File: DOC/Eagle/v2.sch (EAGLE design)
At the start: 18 parts, among them M1 RF-LORA-868-SO, X1 SMA-142-0701-871/876

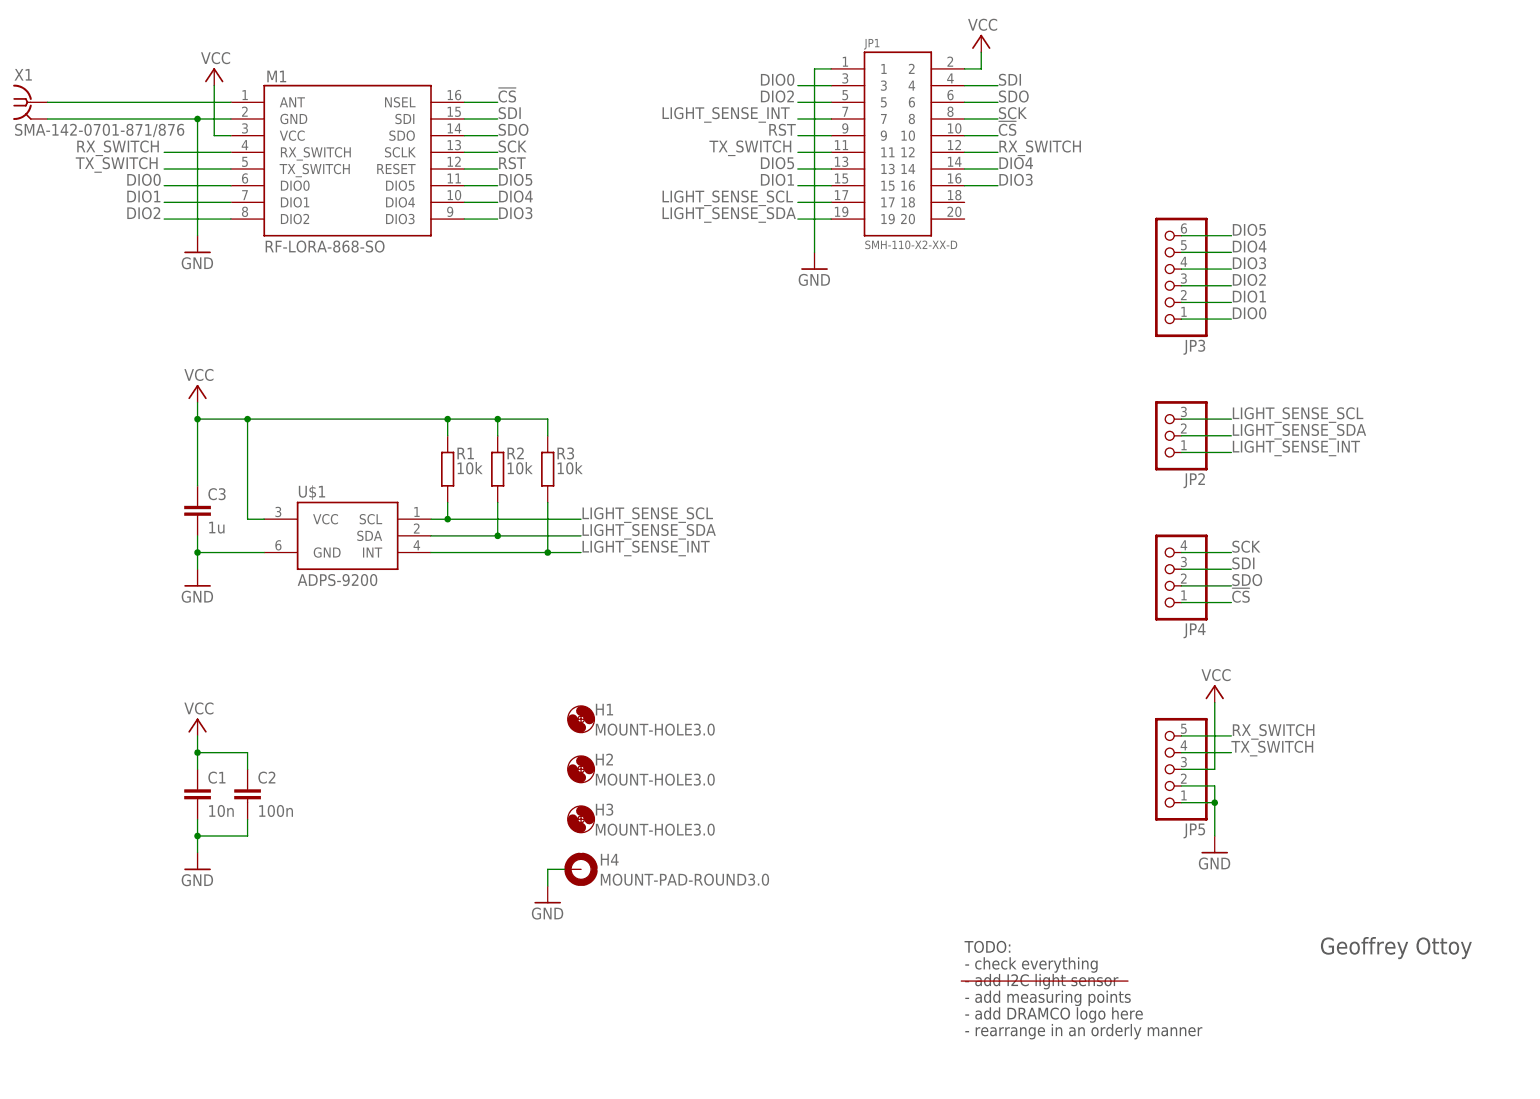
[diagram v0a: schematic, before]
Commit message: Updated hardware design
Finished schematic (final checks needed!)
Included pdf of the schematic
First version of the board (no silkscreen yet)
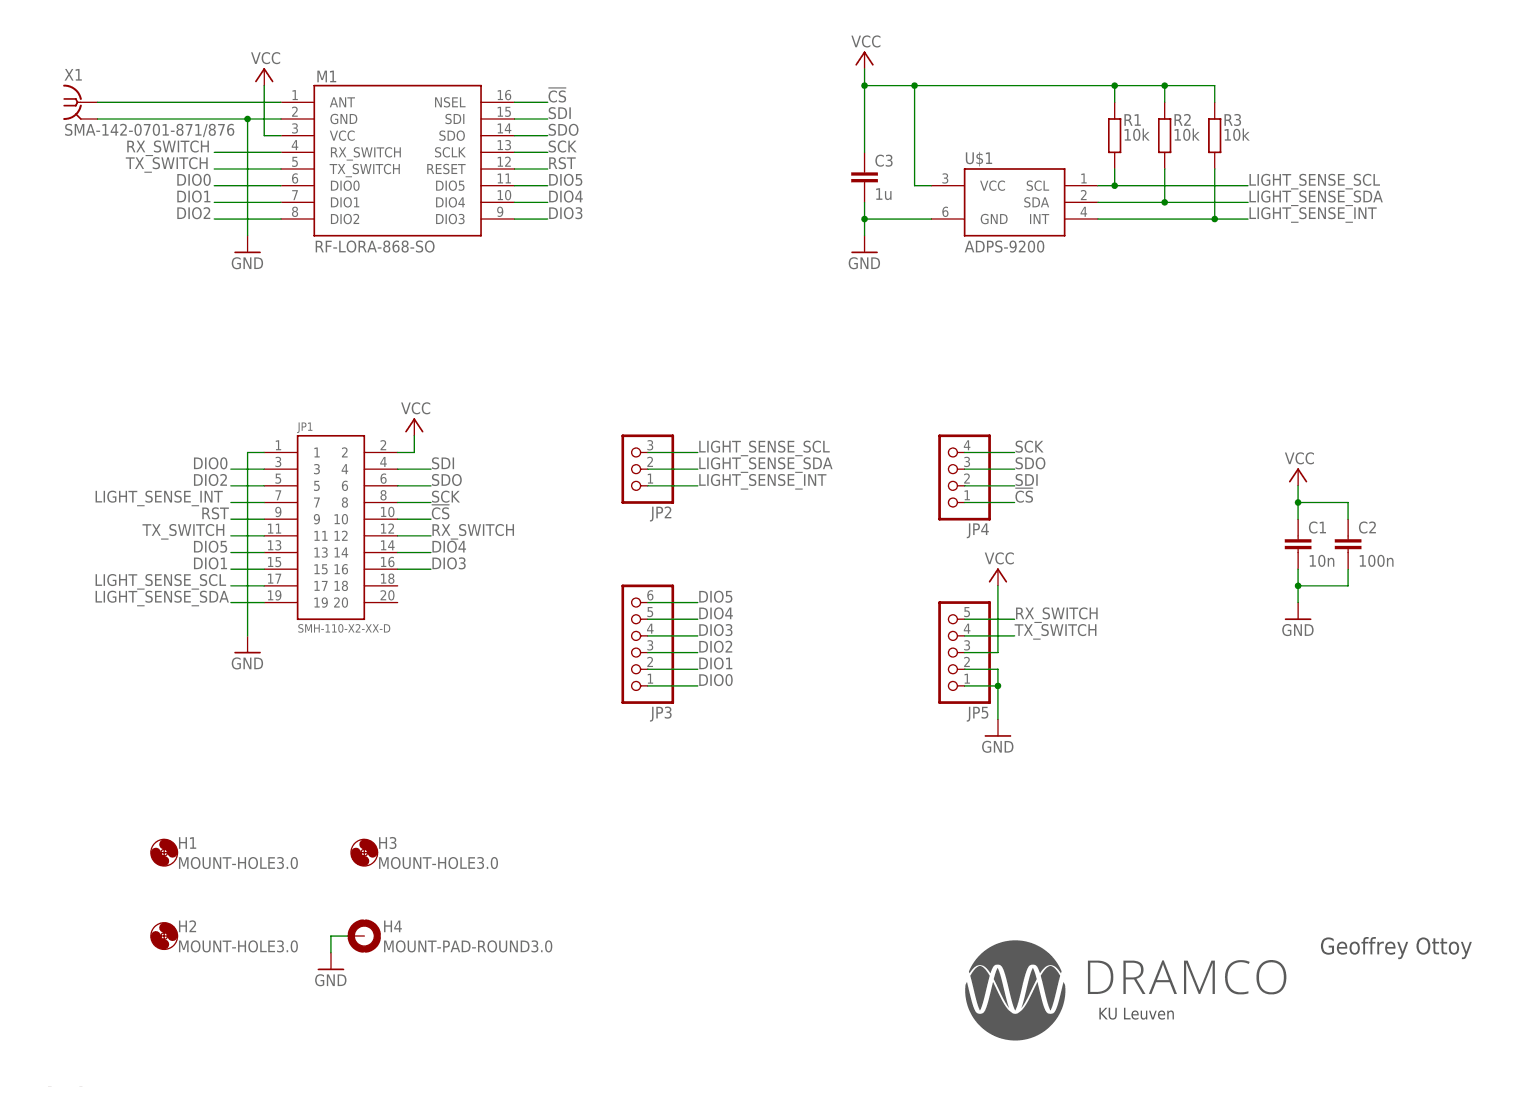
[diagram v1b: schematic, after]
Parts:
- R1, R2, R3: device rcl:R-EU_R1206 -> rcl:R-EU_M0805
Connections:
- net SDI: now also JP4.2; no longer JP4.3
- net SDO: now also JP4.3; no longer JP4.2
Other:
- note added: "KU Leuven"
- note removed: "- add DRAMCO logo here"
- note removed: "- add I2C light sensor"
- note removed: "- add measuring points"
- note removed: "- check everything"
- note removed: "- rearrange in an orderly manner"
- note removed: "TODO:"
- moved on the sheet: C1, C2, C3, H1, H2, H3, H4, JP1, JP2, JP3, JP4, JP5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

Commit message: Updated board design
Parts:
- H1, H2, H3: value MOUNT-HOLE3.0 -> MOUNT-PAD-ROUND3.0; device holes:MOUNT-HOLE3.0 -> holes:MOUNT-PAD-ROUND3.0
- renumbered U$1 to IC1
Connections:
- net GND: now also H1.MOUNT, H2.MOUNT, H3.MOUNT
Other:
- moved on the sheet: H2, H3, H4
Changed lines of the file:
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@@
 </classes>
 <parts>
-<part name="H1" library="holes" library_urn="urn:adsk.eagle:library:237" deviceset="MOUNT-HOLE" device="3.0"/>
-<part name="H2" library="holes" library_urn="urn:adsk.eagle:library:237" deviceset="MOUNT-HOLE" device="3.0"/>
-<part name="H3" library="holes" library_urn="urn:adsk.eagle:library:237" deviceset="MOUNT-HOLE" device="3.0"/>
 <part name="H4" library="holes" library_urn="urn:adsk.eagle:library:237" deviceset="MOUNT-PAD-ROUND" device="3.0"/>
 <part name="GND1" library="supply1" library_urn="urn:adsk.eagle:library:371" deviceset="GND" device=""/>
@@
 <part name="R2" library="rcl" library_urn="urn:adsk.eagle:library:334" deviceset="R-EU_" device="M0805" value="10k"/>
 <part name="R3" library="rcl" library_urn="urn:adsk.eagle:library:334" deviceset="R-EU_" device="M0805" value="10k"/>
-<part name="U$1" library="project" deviceset="ADPS-9200" device=""/>
 <part name="C3" library="rcl" library_urn="urn:adsk.eagle:library:334" deviceset="C-EU" device="C0805K" value="1u"/>
 <part name="GND5" library="supply1" library_urn="urn:adsk.eagle:library:371" deviceset="GND" device=""/>
@@
 <part name="P+5" library="supply1" library_urn="urn:adsk.eagle:library:371" deviceset="VCC" device=""/>
 <part name="GND6" library="supply1" library_urn="urn:adsk.eagle:library:371" deviceset="GND" device=""/>
+<part name="IC1" library="project" deviceset="ADPS-9200" device=""/>
+<part name="H2" library="holes" library_urn="urn:adsk.eagle:library:237" deviceset="MOUNT-PAD-ROUND" device="3.0"/>
+<part name="H3" library="holes" library_urn="urn:adsk.eagle:library:237" deviceset="MOUNT-PAD-ROUND" device="3.0"/>
+<part name="H1" library="holes" library_urn="urn:adsk.eagle:library:237" deviceset="MOUNT-PAD-ROUND" device="3.0"/>
+<part name="GND7" library="supply1" library_urn="urn:adsk.eagle:library:371" deviceset="GND" device=""/>
+<part name="GND8" library="supply1" library_urn="urn:adsk.eagle:library:371" deviceset="GND" device=""/>
+<part name="GND9" library="supply1" library_urn="urn:adsk.eagle:library:371" deviceset="GND" device=""/>
 </parts>
 <sheets>
@@
 </plain>
 <instances>
-<instance part="H1" gate="G$1" x="40.64" y="35.56"/>
-<instance part="H2" gate="G$1" x="40.64" y="22.86"/>
-<instance part="H3" gate="G$1" x="71.12" y="35.56"/>
-<instance part="H4" gate="G$1" x="71.12" y="22.86"/>
-<instance part="GND1" gate="1" x="66.04" y="17.78"/>
+<instance part="H4" gate="G$1" x="78.74" y="22.86"/>
+<instance part="GND1" gate="1" x="73.66" y="17.78"/>
 <instance part="JP1" gate="G$1" x="66.04" y="86.36"/>
 <instance part="GND2" gate="1" x="53.34" y="66.04"/>
@@
 <attribute name="VALUE" x="201.93" y="144.018" size="1.778" layer="96"/>
 </instance>
-<instance part="U$1" gate="G$1" x="170.18" y="134.62"/>
 <instance part="C3" gate="G$1" x="147.32" y="139.7"/>
 <instance part="GND5" gate="1" x="147.32" y="127"/>
@@
 </instance>
 <instance part="GND6" gate="1" x="167.64" y="53.34"/>
+<instance part="IC1" gate="G$1" x="170.18" y="134.62"/>
+<instance part="H2" gate="G$1" x="78.74" y="35.56"/>
+<instance part="H3" gate="G$1" x="40.64" y="22.86"/>
+<instance part="H1" gate="G$1" x="40.64" y="35.56"/>
+<instance part="GND7" gate="1" x="73.66" y="30.48"/>
+<instance part="GND8" gate="1" x="35.56" y="30.48"/>
+<instance part="GND9" gate="1" x="35.56" y="17.78"/>
 </instances>
 <busses>
@@
 <pinref part="H4" gate="G$1" pin="MOUNT"/>
 <pinref part="GND1" gate="1" pin="GND"/>
-<wire x1="68.58" y1="22.86" x2="66.04" y2="22.86" width="0.1524" layer="91"/>
-<wire x1="66.04" y1="22.86" x2="66.04" y2="20.32" width="0.1524" layer="91"/>
+<wire x1="76.2" y1="22.86" x2="73.66" y2="22.86" width="0.1524" layer="91"/>
+<wire x1="73.66" y1="22.86" x2="73.66" y2="20.32" width="0.1524" layer="91"/>
 </segment>
 <segment>
@@
 </segment>
 <segment>
-<pinref part="U$1" gate="G$1" pin="GND"/>
 <wire x1="157.48" y1="132.08" x2="147.32" y2="132.08" width="0.1524" layer="91"/>
 <pinref part="C3" gate="G$1" pin="2"/>
@@
 <wire x1="147.32" y1="129.54" x2="147.32" y2="132.08" width="0.1524" layer="91"/>
 <junction x="147.32" y="132.08"/>
+<pinref part="IC1" gate="G$1" pin="GND"/>
 </segment>
 <segment>
@@
 <pinref part="GND6" gate="1" pin="GND"/>
 </segment>
+<segment>
+<pinref part="H3" gate="G$1" pin="MOUNT"/>
+<pinref part="GND9" gate="1" pin="GND"/>
+<wire x1="38.1" y1="22.86" x2="35.56" y2="22.86" width="0.1524" layer="91"/>
+<wire x1="35.56" y1="22.86" x2="35.56" y2="20.32" width="0.1524" layer="91"/>
+</segment>
+<segment>
+<pinref part="H1" gate="G$1" pin="MOUNT"/>
+<pinref part="GND8" gate="1" pin="GND"/>
+<wire x1="38.1" y1="35.56" x2="35.56" y2="35.56" width="0.1524" layer="91"/>
+<wire x1="35.56" y1="35.56" x2="35.56" y2="33.02" width="0.1524" layer="91"/>
+</segment>
+<segment>
+<pinref part="H2" gate="G$1" pin="MOUNT"/>
+<pinref part="GND7" gate="1" pin="GND"/>
+<wire x1="76.2" y1="35.56" x2="73.66" y2="35.56" width="0.1524" layer="91"/>
+<wire x1="73.66" y1="35.56" x2="73.66" y2="33.02" width="0.1524" layer="91"/>
+</segment>
 </net>
 <net name="VCC" class="0">
@@
 </segment>
 <segment>
-<pinref part="U$1" gate="G$1" pin="VCC"/>
 <wire x1="157.48" y1="137.16" x2="154.94" y2="137.16" width="0.1524" layer="91"/>
 <wire x1="154.94" y1="137.16" x2="154.94" y2="152.4" width="0.1524" layer="91"/>
@@
 <wire x1="147.32" y1="152.4" x2="147.32" y2="154.94" width="0.1524" layer="91"/>
 <junction x="147.32" y="152.4"/>
+<pinref part="IC1" gate="G$1" pin="VCC"/>
 </segment>
 <segment>
@@
 <net name="LIGHT_SENSE_SCL" class="0">
 <segment>
-<pinref part="U$1" gate="G$1" pin="SCL"/>
 <wire x1="182.88" y1="137.16" x2="185.42" y2="137.16" width="0.1524" layer="91"/>
 <pinref part="R1" gate="G$1" pin="1"/>
@@
 <junction x="185.42" y="137.16"/>
 <label x="205.74" y="137.16" size="1.778" layer="95"/>
+<pinref part="IC1" gate="G$1" pin="SCL"/>
 </segment>
 <segment>
@@
 <net name="LIGHT_SENSE_SDA" class="0">
 <segment>
-<pinref part="U$1" gate="G$1" pin="SDA"/>
 <wire x1="182.88" y1="134.62" x2="193.04" y2="134.62" width="0.1524" layer="91"/>
 <pinref part="R2" gate="G$1" pin="1"/>
@@
 <junction x="193.04" y="134.62"/>
 <label x="205.74" y="134.62" size="1.778" layer="95"/>
+<pinref part="IC1" gate="G$1" pin="SDA"/>
 </segment>
 <segment>
@@
 <net name="LIGHT_SENSE_INT" class="0">
 <segment>
-<pinref part="U$1" gate="G$1" pin="INT"/>
 <wire x1="182.88" y1="132.08" x2="200.66" y2="132.08" width="0.1524" layer="91"/>
 <pinref part="R3" gate="G$1" pin="1"/>
@@
 <junction x="200.66" y="132.08"/>
 <label x="205.74" y="132.08" size="1.778" layer="95"/>
+<pinref part="IC1" gate="G$1" pin="INT"/>
 </segment>
 <segment>

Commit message: Final touches to board design, Gerber files
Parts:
- H1, H2, H3, H4: value MOUNT-PAD-ROUND3.0 -> MOUNT-HOLE3.0; device holes:MOUNT-PAD-ROUND3.0 -> holes:MOUNT-HOLE3.0
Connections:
- net GND: no longer H1.MOUNT, H2.MOUNT, H3.MOUNT, H4.MOUNT
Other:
- moved on the sheet: H1, H2, H3, H4
